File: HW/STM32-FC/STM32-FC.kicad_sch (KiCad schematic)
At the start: 34 parts, among them J1 GH 1.25mm 6P, Q1 PMDPB30XN, U1 STM32F407VETx, Y1 16MHz

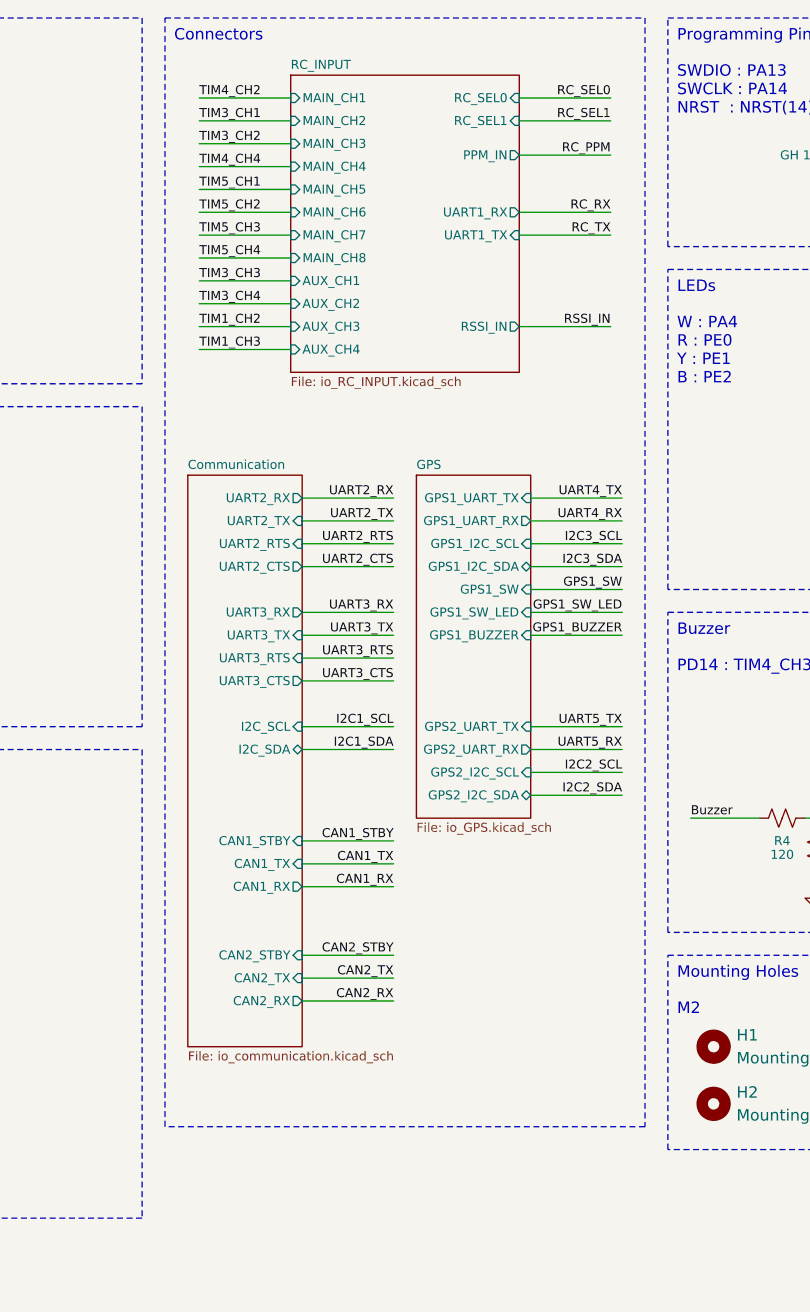
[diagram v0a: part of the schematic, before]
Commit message: HW Lib and RC code refactoring, GCS_log united and BMI323 IMU init.
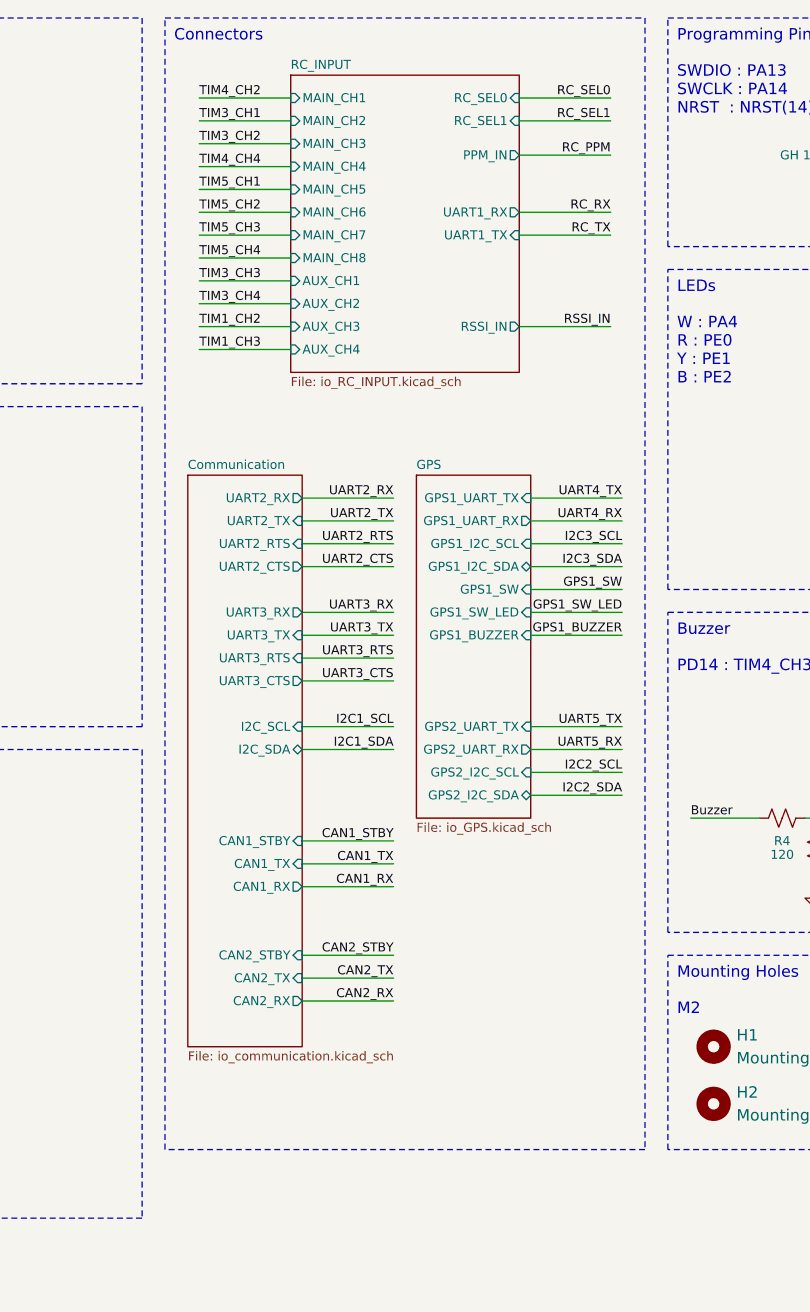
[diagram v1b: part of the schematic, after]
